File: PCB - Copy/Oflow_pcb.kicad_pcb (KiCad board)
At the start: 2 copper layers, 105 x 85 mm, 56 parts, among them J1 Conn_01x04, J2 Conn_01x03, J3 Conn_01x02, J4 Conn_01x02, K1 RAYEX-L90, Q1 BC547, Q4 2N2219, Q5 BC547, U1 PIC16F676-I_P, U1 node, U2 L7805

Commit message: added nod
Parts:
- removed R11, R13: R, MyLib:R_Axial_DIN0207_L6.3mm_D2.5mm_P10.16mm_Horizontal
- removed the U1 at (94.1, 76.6)
- removed the U1 at (167.6, 78.7)
- added U1: NodeMCU, NodeMCU:NODE V1, F.Cu at (74.3, 48.9)
- K1: footprint myLib:Relay_SPDT_RAYEX-L90 -> Relay_THT:Relay_SPDT_RAYEX-L90
- Q1: footprint MyLib:TO-92_Inline_Wide -> Package_TO_SOT_THT:TO-92_Inline
- Q4, Q5: footprint MyLib:TO-92_Inline_Wide -> Package_TO_SOT_THT:TO-92L_Wide
- R1, R10, R12, R14, R15, R18, R20, R8, R9: footprint MyLib:R_Axial_DIN0207_L6.3mm_D2.5mm_P10.16mm_Horizontal -> Resistor_THT:R_Axial_DIN0207_L6.3mm_D2.5mm_P10.16mm_Horizontal
- R16: value 330R -> 56K; footprint MyLib:R_Axial_DIN0207_L6.3mm_D2.5mm_P10.16mm_Horizontal -> Resistor_THT:R_Axial_DIN0207_L6.3mm_D2.5mm_P10.16mm_Horizontal
- R17: value 330R -> 15K; footprint MyLib:R_Axial_DIN0207_L6.3mm_D2.5mm_P10.16mm_Horizontal -> Resistor_THT:R_Axial_DIN0207_L6.3mm_D2.5mm_P10.16mm_Horizontal
- R19: value 330R -> 10K; footprint MyLib:R_Axial_DIN0207_L6.3mm_D2.5mm_P10.16mm_Horizontal -> Resistor_THT:R_Axial_DIN0207_L6.3mm_D2.5mm_P10.16mm_Horizontal
- R2: value 330R -> 10K
- R3, R4: value 330R -> 1K; footprint MyLib:R_Axial_DIN0207_L6.3mm_D2.5mm_P10.16mm_Horizontal -> Resistor_THT:R_Axial_DIN0207_L6.3mm_D2.5mm_P10.16mm_Horizontal
- R5: value 10k -> 10K
- R7: value 100k -> 68K; footprint MyLib:R_Axial_DIN0207_L6.3mm_D2.5mm_P10.16mm_Horizontal -> Resistor_THT:R_Axial_DIN0207_L6.3mm_D2.5mm_P10.16mm_Horizontal
- moved C2 29.4 mm to (67.5, 84.5)
- moved D14 28.7 mm to (52.5, 65.7), turned to 0 degrees
- moved C8 25.8 mm to (68.4, 71.5)
- moved Q5 21.1 mm to (106.7, 63.4)
- moved C1 20.9 mm to (67.7, 78.1)
- moved R14 16.2 mm to (49.0, 62.8)
- moved J4 16.1 mm to (55.6, 74.2)
- moved R18 15.5 mm to (48.8, 76.4)
- moved D13 15.2 mm to (64.0, 60.4)
- moved R15 15.2 mm to (48.6, 72.9)
- moved R17 14.7 mm to (49.1, 57.9)
- moved C7 14.0 mm to (68.4, 66.8)
- moved BZ1 8.64 mm to (60.8, 52.8)
- moved R16 7.41 mm to (46.4, 52.9)
- moved R9 6.54 mm to (108.7, 55.9)
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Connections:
- R10 pad 1: C3 -> D1
- R12 pad 1: C1 -> D3
- R14 pad 1: A0 -> D5
- R18 pad 1: A5 -> s2
- R8 pad 2: C0 -> D6
- R9 pad 1: C2 -> D0
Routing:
- net A5: track 45.3 -> 0.00 mm
- net s3: track 45.0 -> 0.00 mm
- net D8: track 44.2 -> 0.00 mm
- net C0: track 42.4 -> 0.00 mm
- net D7: track 40.9 -> 0.00 mm
- net C1: track 36.7 -> 0.00 mm
- net A0: track 41.2 -> 5.68 mm
- net +5V: track 173.5 -> 139.2 mm
- net A1: track 27.3 -> 0.00 mm
- net Net-(C3-Pad1): track 44.7 -> 22.3 mm
- net Net-(D6-Pad2): track 21.9 -> 0.00 mm
- net +12V: track 204.9 -> 183.2 mm
- net C2: track 19.7 -> 0.00 mm
- net Net-(Q5-Pad2): track 17.6 -> 0.00 mm
- net C3: track 17.2 -> 0.00 mm
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
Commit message: l
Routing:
- net +5V: track 139.2 -> 79.5 mm
- net +3.3V: track 0.00 -> 32.1 mm
- net Net-(D8-Pad2): track 16.4 -> 2.69 mm
- net +12V: track 183.2 -> 170.3 mm
- net GND: track 5.71 -> 16.9 mm
- net A0: track 5.68 -> 0.00 mm
- net s3: track 0.00 -> 5.38 mm
- net Net-(D7-Pad2): track 11.4 -> 7.27 mm
- net D5: track 1.52 -> 0.00 mm
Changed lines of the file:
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@@
   (via locked (at 129.09862 48.97424) (size 4) (drill 3) (layers "F.Cu" "B.Cu") (net 0))
   (via locked (at 54.09862 48.47424) (size 4) (drill 3) (layers "F.Cu" "B.Cu") (net 0))
-  (segment (start 38.95 57.89) (end 39.64862 57.19138) (width 0.8) (layer "B.Cu") (net 1))
-  (segment (start 39.64862 57.19138) (end 39.64862 52.47424) (width 0.8) (layer "B.Cu") (net 1))
+  (segment (start 74.35 100.23) (end 79.3 100.23) (width 0.8) (layer "B.Cu") (net 1))
+  (segment (start 39.64862 52.47424) (end 39.64862 57.19138) (width 0.8) (layer "B.Cu") (net 1))
+  (segment (start 59.61634 98.40366) (end 56.9 101.12) (width 0.8) (layer "B.Cu") (net 1))
+  (segment (start 79.3 100.23) (end 79.425 100.355) (width 0.8) (layer "B.Cu") (net 1))
+  (segment (start 39.64862 57.19138) (end 38.95 57.89) (width 0.8) (layer "B.Cu") (net 1))
+  (segment (start 59.61634 96.1479) (end 59.61634 98.40366) (width 0.8) (layer "B.Cu") (net 1))
   (segment (start 129.865 55.435) (end 132.785 55.435) (width 1) (layer "B.Cu") (net 2))
   (segment (start 132.785 55.435) (end 134.93 57.58) (width 1) (layer "B.Cu") (net 2))
@@
   (segment (start 42.3 88.57884) (end 43.50508 87.37376) (width 0.8) (layer "B.Cu") (net 3))
   (segment (start 110.49048 97.03452) (end 110.49048 77.16548) (width 1) (layer "B.Cu") (net 3))
-  (segment (start 46.29702 82.438867) (end 46.29702 82.30298) (width 0.8) (layer "B.Cu") (net 3))
-  (segment (start 51.5 77.1) (end 54.472262 77.1) (width 0.8) (layer "B.Cu") (net 3))
   (segment (start 62.7 108.2) (end 67.575 113.075) (width 1) (layer "B.Cu") (net 3))
   (segment (start 103.4 104.125) (end 110.49048 97.03452) (width 1) (layer "B.Cu") (net 3))
@@
   (segment (start 47.633333 102.32) (end 52.366666 102.32) (width 2) (layer "B.Cu") (net 3))
   (segment (start 110.49048 77.16548) (end 109.488034 76.163034) (width 1) (layer "B.Cu") (net 3))
-  (segment (start 54.472262 77.1) (end 56.24 75.332262) (width 0.8) (layer "B.Cu") (net 3))
   (segment (start 44.7616 95.61724) (end 42.3 93.15564) (width 0.8) (layer "B.Cu") (net 3))
   (segment (start 121.8 69.325) (end 124.000489 71.525489) (width 1) (layer "B.Cu") (net 3))
   (segment (start 47.633333 102.32) (end 47.633333 96.548493) (width 2) (layer "B.Cu") (net 3))
   (segment (start 109.488034 76.163034) (end 109.488034 70.736966) (width 1) (layer "B.Cu") (net 3))
-  (segment (start 46.29702 82.30298) (end 51.5 77.1) (width 0.8) (layer "B.Cu") (net 3))
   (segment (start 110.9 69.325) (end 121.8 69.325) (width 1) (layer "B.Cu") (net 3))
   (segment (start 45.025 83.710887) (end 46.29702 82.438867) (width 0.8) (layer "B.Cu") (net 3))
@@
   (segment (start 67.3616 116.7866) (end 66.825 116.25) (width 3) (layer "B.Cu") (net 12))
   (segment (start 67.3616 122.71724) (end 67.3616 116.7866) (width 3) (layer "B.Cu") (net 12))
-  (segment (start 63.7216 59.95724) (end 67.7366 63.97224) (width 1) (layer "B.Cu") (net 13))
   (segment (start 110.5366 52.61724) (end 108.2 54.95384) (width 0.6) (layer "B.Cu") (net 15))
   (segment (start 113.0616 52.61724) (end 110.5366 52.61724) (width 0.6) (layer "B.Cu") (net 15))
@@
   (segment (start 114.445 74.175) (end 119.14862 78.87862) (width 0.6) (layer "B.Cu") (net 21))
   (segment (start 112.93 74.175) (end 114.445 74.175) (width 0.6) (layer "B.Cu") (net 21))
-  (segment (start 42.56532 68.54444) (end 42.7609 68.74002) (width 0.8) (layer "B.Cu") (net 22))
-  (segment (start 42.7609 68.74002) (end 52.68438 68.74002) (width 0.8) (layer "B.Cu") (net 22))
-  (segment (start 52.68438 68.74002) (end 53.5616 69.61724) (width 0.8) (layer "B.Cu") (net 22))
-  (segment (start 42.6212 81.79764) (end 49.3016 75.11724) (width 0.8) (layer "B.Cu") (net 23))
+  (segment (start 38.83 62.79) (end 42.64862 66.60862) (width 0.8) (layer "B.Cu") (net 22))
+  (segment (start 42.64862 66.60862) (end 42.64862 68.47424) (width 0.8) (layer "B.Cu") (net 22))
   (segment (start 42.6212 84.44682) (end 42.64862 84.47424) (width 0.8) (layer "B.Cu") (net 23))
-  (segment (start 49.3016 75.11724) (end 53.5616 75.11724) (width 0.8) (layer "B.Cu") (net 23))
   (segment (start 42.6212 81.79764) (end 42.6212 84.44682) (width 0.8) (layer "B.Cu") (net 23))
-  (segment (start 52.0616 82.5784) (end 53.64 81) (width 1) (layer "B.Cu") (net 25))
-  (segment (start 54.67884 81) (end 60.5616 75.11724) (width 1) (layer "B.Cu") (net 25))
-  (segment (start 61.0616 74.61724) (end 63.5616 74.61724) (width 1) (layer "B.Cu") (net 25))
   (segment (start 58.11724 84.61724) (end 58.21724 84.61724) (width 0.8) (layer "B.Cu") (net 25))
   (segment (start 66.425 92.825) (end 66.425 105.69) (width 0.8) (layer "B.Cu") (net 25))
-  (segment (start 53.64 81) (end 54.67884 81) (width 1) (layer "B.Cu") (net 25))
   (segment (start 95.825 104.1) (end 89.425 110.5) (width 0.6) (layer "B.Cu") (net 25))
   (segment (start 50.920798 84.61724) (end 52.5616 84.61724) (width 2) (layer "B.Cu") (net 25))
-  (segment (start 63.614 49.276) (end 68.28 44.61) (width 0.6) (layer "B.Cu") (net 25))
-  (segment (start 60.1366 75.54224) (end 60.1366 73.3446) (width 0.6) (layer "B.Cu") (net 25))
   (segment (start 66.425 105.69) (end 66.825 106.09) (width 0.8) (layer "B.Cu") (net 25))
   (segment (start 47.0616 88.476438) (end 50.920798 84.61724) (width 2) (layer "B.Cu") (net 25))
@@
   (segment (start 70.825 110.5) (end 66.825 106.5) (width 0.6) (layer "B.Cu") (net 25))
   (segment (start 47.0616 90.11724) (end 47.0616 88.476438) (width 2) (layer "B.Cu") (net 25))
-  (segment (start 60.1366 73.3446) (end 58.928 72.136) (width 0.6) (layer "B.Cu") (net 25))
   (segment (start 58.21724 84.61724) (end 66.425 92.825) (width 0.8) (layer "B.Cu") (net 25))
   (segment (start 95.825 100.78) (end 95.825 104.1) (width 0.6) (layer "B.Cu") (net 25))
-  (segment (start 60.5616 75.11724) (end 61.0616 74.61724) (width 1) (layer "B.Cu") (net 25))
-  (segment (start 60.96 49.276) (end 63.614 49.276) (width 0.6) (layer "B.Cu") (net 25))
-  (segment (start 58.928 72.136) (end 58.928 51.308) (width 0.6) (layer "B.Cu") (net 25))
   (segment (start 89.425 110.5) (end 70.825 110.5) (width 0.6) (layer "B.Cu") (net 25))
-  (segment (start 58.928 51.308) (end 60.96 49.276) (width 0.6) (layer "B.Cu") (net 25))
   (segment (start 51.5616 84.61724) (end 58.11724 84.61724) (width 1) (layer "B.Cu") (net 25))
-  (segment (start 63.7216 74.61724) (end 71.19224 74.61724) (width 0.6) (layer "B.Cu") (net 25))
-  (segment (start 60.5616 75.11724) (end 60.1366 75.54224) (width 0.6) (layer "B.Cu") (net 25))
   (segment (start 52.0616 84.61724) (end 52.0616 82.5784) (width 1) (layer "B.Cu") (net 25))
   (segment (start 82.70611 103.4) (end 88.225 103.4) (width 0.6) (layer "B.Cu") (net 26))
@@
   (segment (start 86.05 117.15) (end 86.05 116.505) (width 3) (layer "B.Cu") (net 30))
   (segment (start 82.6016 120.5984) (end 86.05 117.15) (width 3) (layer "B.Cu") (net 30))
+  (segment (start 68.975 90.07) (end 74.35 90.07) (width 0.8) (layer "B.Cu") (net 31))
   (segment (start 118.025 105.1) (end 113.675 105.1) (width 0.6) (layer "B.Cu") (net 33))
   (segment (start 111.85 79.655) (end 113.005 78.5) (width 0.6) (layer "B.Cu") (net 33))
@@
   (segment (start 113.675 105.1) (end 111.8 103.225) (width 0.6) (layer "B.Cu") (net 33))
   (segment (start 119.14862 101.47424) (end 119.14862 103.97638) (width 0.6) (layer "B.Cu") (net 33))
-  (segment (start 42.68978 52.48148) (end 42.6212 52.55006) (width 0.8) (layer "B.Cu") (net 34))
-  (segment (start 63.7216 69.61724) (end 64.7966 70.69224) (width 0.6) (layer "B.Cu") (net 38))
+  (segment (start 92.128 74.29) (end 102.288 84.45) (width 0.8) (layer "B.Cu") (net 46))
+  (segment (start 74.348 74.29) (end 92.128 74.29) (width 0.8) (layer "B.Cu") (net 46))
   (zone (net 1) (net_name "GND") (layer "B.Cu") (hatch edge 0.508)
     (connect_pads (clearance 0.5))

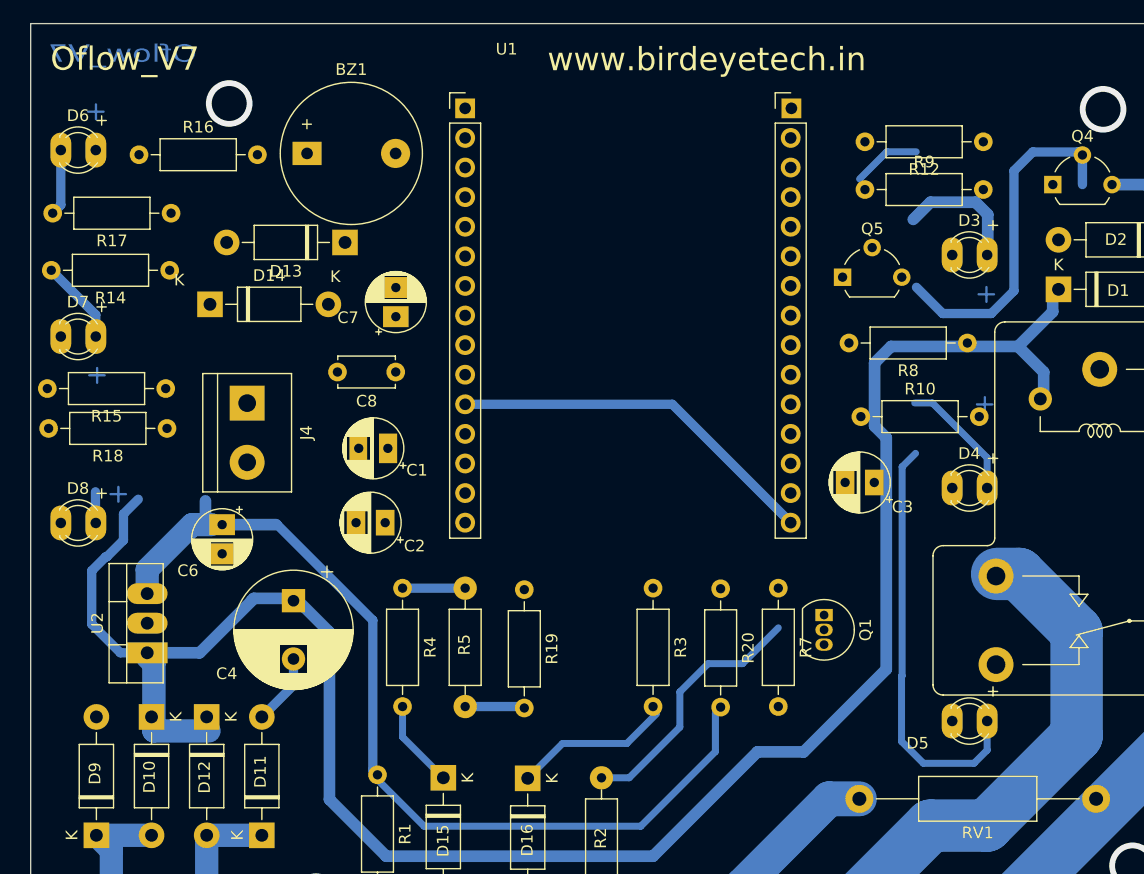
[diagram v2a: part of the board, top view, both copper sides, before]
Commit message: foot print changed
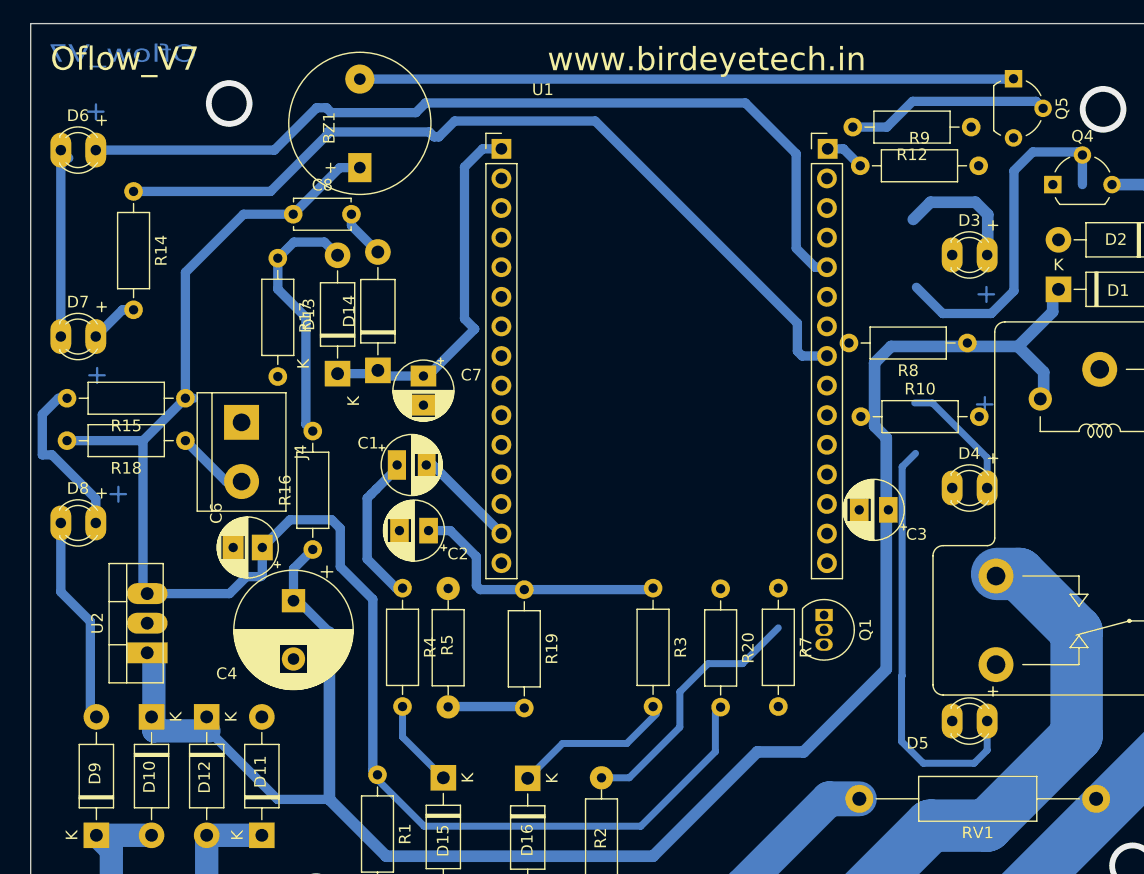
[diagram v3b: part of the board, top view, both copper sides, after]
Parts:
- moved R16 37.0 mm to (61.3, 86.8), turned to 90 degrees
- moved Q5 22.5 mm to (121.4, 46.4), turned to -90 degrees
- moved C8 16.1 mm to (59.6, 58.0), turned to 0 degrees
- moved D14 15.5 mm to (66.9, 71.4), turned to 90 degrees
- moved D13 11.3 mm to (63.4, 71.7), turned to 90 degrees
- moved R17 9.94 mm to (58.3, 61.8), turned to -90 degrees
- moved R14 7.45 mm to (45.9, 56.0), turned to -90 degrees
- moved C7 5.62 mm to (70.8, 71.9), turned to -90 degrees
- moved BZ1 4.69 mm to (65.3, 54.0), turned to 90 degrees
- moved U1 4.66 mm to (77.5, 52.4)
- moved C6 3.97 mm to (56.9, 86.6), turned to 180 degrees
- moved C2 3.79 mm to (71.2, 85.1)
- moved C3 2.64 mm to (110.7, 83.3)
- moved R9 2.08 mm to (108.3, 53.8)
- moved R18 1.90 mm to (50.3, 77.4)
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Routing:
- net D4: track 0.00 -> 76.0 mm
- net D5: track 0.00 -> 72.2 mm
- net Net-(BZ1-Pad2): track 0.00 -> 56.1 mm
- net +5V: track 79.5 -> 135.5 mm
- net GND: track 16.9 -> 54.5 mm
- net +3.3V: track 32.1 -> 0.00 mm
- net A0: track 0.00 -> 31.8 mm
- net D8: track 0.00 -> 22.9 mm
- net Net-(D13-Pad2): track 0.00 -> 22.3 mm
- net Net-(Q5-Pad2): track 0.00 -> 17.5 mm
- net +12V: track 170.3 -> 154.5 mm
- net Net-(D8-Pad2): track 2.69 -> 14.4 mm
- net s3: track 5.38 -> 13.2 mm
- net s2: track 0.00 -> 6.27 mm
- net Net-(D7-Pad2): track 7.27 -> 4.19 mm
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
